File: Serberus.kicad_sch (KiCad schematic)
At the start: 108 parts, among them J1 USB_C_Receptacle_USB2.0, J2 UART 1,3,4, J3 SWD/JTAG2, J4 LA, J5 SPI, J6 CORTEX, J7 I2C, J8 iCE40, J9 V_Merge, Q1 BSH103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

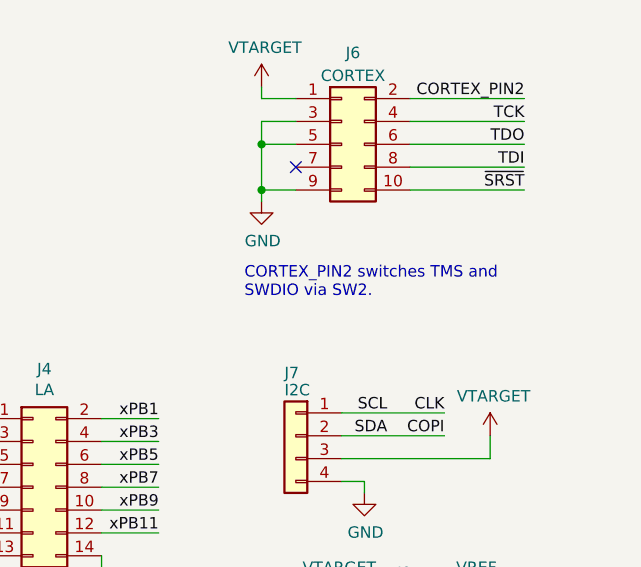
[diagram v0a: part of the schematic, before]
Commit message: Update Serberus.kicad_sch
Updated part numbers
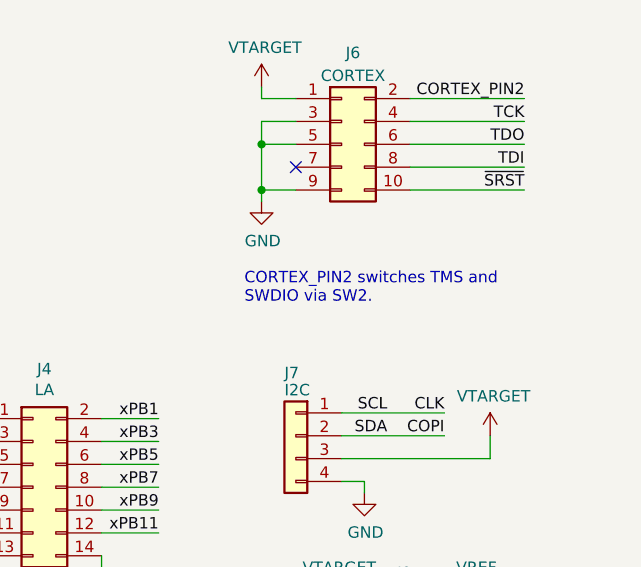
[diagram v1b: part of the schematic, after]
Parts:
- J4: P/N FTSH-107-01-F-DV-K -> 77313-103-14LF
- SW1: Manufacturer_Part_Number NR01105ANG13-2A -> NR01104ANG13-2A; Mouser Part Number 633-NR01105ANG13-2A -> 633-NR01104ANG13-2A
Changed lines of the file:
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@@
     (effects (font (size 1.27 1.27)) (justify left bottom))
   )
-  (text "CORTEX_PIN2 switches TMS and\nSWDIO via SW2. \n" (at 370.205 74.295 0)
+  (text "CORTEX_PIN2 switches TMS and\nSWDIO via SW2. \n" (at 370.205 74.93 0)
     (effects (font (size 1.27 1.27)) (justify left bottom))
   )
@@
       (effects (font (size 1.27 1.27)) hide)
     )
-    (property "Manufacturer_Part_Number" "NR01105ANG13-2A" (at 362.585 144.145 0)
+    (property "Manufacturer_Part_Number" "NR01104ANG13-2A" (at 362.585 144.145 0)
       (effects (font (size 1.27 1.27)) hide)
     )
@@
       (effects (font (size 1.27 1.27)) hide)
     )
-    (property "Mouser Part Number" "633-NR01105ANG13-2A" (at 349.885 153.035 0)
+    (property "Mouser Part Number" "633-NR01104ANG13-2A" (at 349.885 153.035 0)
       (effects (font (size 2.54 2.54)) hide)
     )
@@
       (effects (font (size 1.27 1.27)) hide)
     )
-    (property "P/N" "FTSH-107-01-F-DV-K" (at 346.71 95.25 0)
-      (effects (font (size 1.27 1.27)) hide)
-    )
+    (property "P/N" "77313-103-14LF" (at 346.71 95.25 0)
+      (effects (font (size 1.27 1.27)) hide)
+    )
